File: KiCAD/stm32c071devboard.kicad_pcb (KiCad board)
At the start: 2 copper layers, 38.4 x 19.2 mm, 24 parts, among them J1 USB_C_Receptacle_USB2.0_14P, J2 Conn_01x14_Pin, J3 Conn_01x01_Pin, J4 Conn_01x14_Pin, J5 Conn_01x02_Pin, U1 STM32C071G8UxN, U3 TPS73633DBV

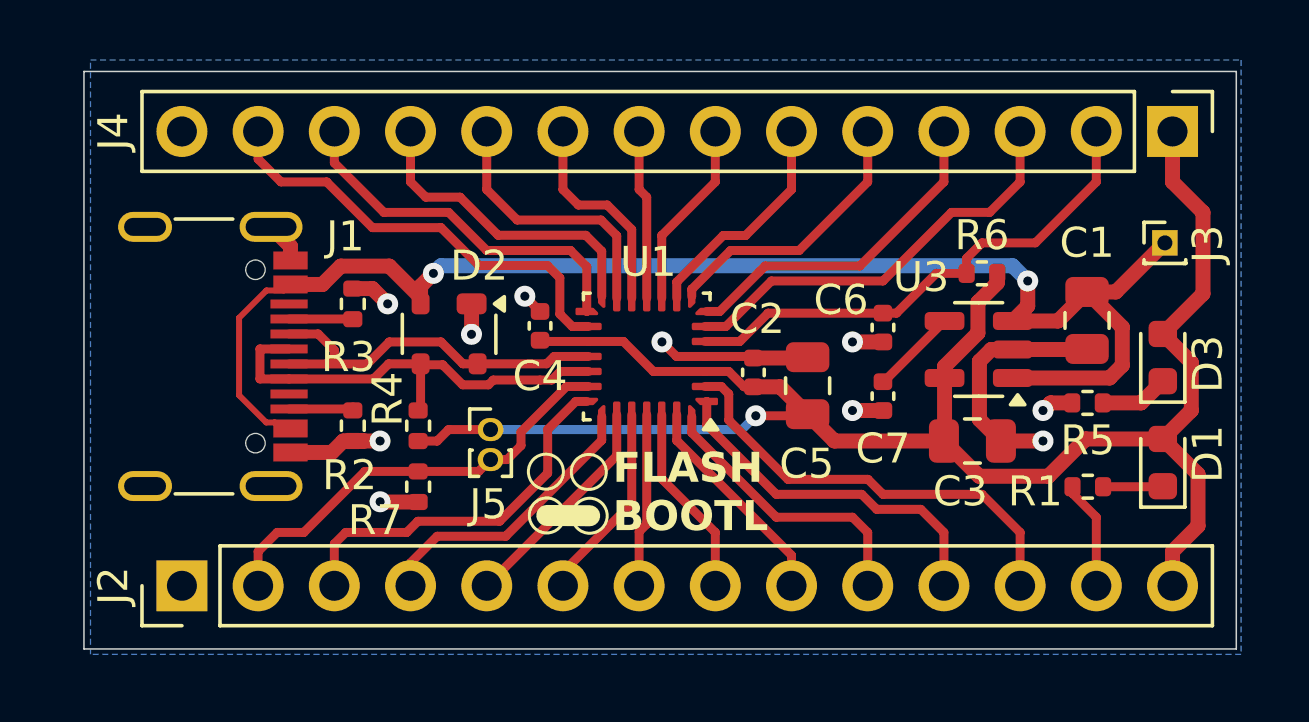
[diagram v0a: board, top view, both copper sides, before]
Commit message: Fixed 2 pins
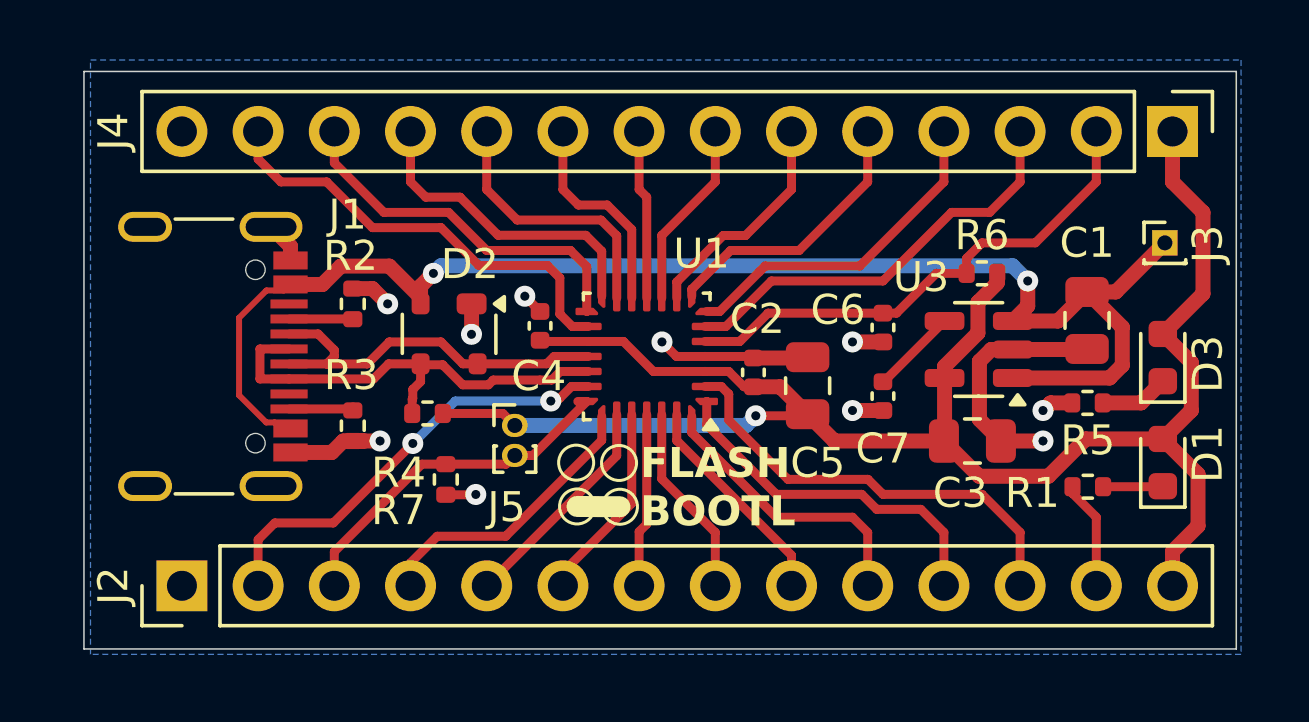
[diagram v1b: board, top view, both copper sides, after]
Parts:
- moved R7 0.95 mm to (91.6, 69.1)
- moved J5 0.82 mm to (93.9, 67.3)
- moved R4 0.52 mm to (91.0, 66.9), turned to 0 degrees
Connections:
- J2 pad 2: BOOT0 -> PA13
- J2 pad 3: PA13 -> BOOT0
- U1 pad 20: BOOT0 -> PA13
- U1 pad 21: PA13 -> BOOT0
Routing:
- net BOOT0: track 14.7 -> 11.9 mm
- net PA13: track 12.6 -> 14.9 mm, vias 0 -> 2
- net +3V3: track 60.7 -> 59.8 mm

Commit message: Minor mods
Top level ground plane and a few stitching vias
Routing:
- net GND: vias 10 -> 21
- added copper zone on F.Cu, net GND
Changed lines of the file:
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@@
+	)
+	(via
+		(at 83.525 65.278)
+		(size 0.7)
+		(drill 0.3)
+		(layers "F.Cu" "B.Cu")
+		(free yes)
+		(net 1)
 	)
 	(via
@@
 	)
 	(via
+		(at 80.985 67.818)
+		(size 0.7)
+		(drill 0.3)
+		(layers "F.Cu" "B.Cu")
+		(free yes)
+		(net 1)
+	)
+	(via
 		(at 111.506 66.802)
 		(size 0.7)
@@
 	)
 	(via
+		(at 83.525 67.818)
+		(size 0.7)
+		(drill 0.3)
+		(layers "F.Cu" "B.Cu")
+		(free yes)
+		(net 1)
+	)
+	(via
 		(at 98.806 64.516)
 		(size 0.7)
@@
 	)
 	(via
+		(at 83.525 62.738)
+		(size 0.7)
+		(drill 0.3)
+		(layers "F.Cu" "B.Cu")
+		(free yes)
+		(net 1)
+	)
+	(via
 		(at 89.662 63.246)
 		(size 0.7)
@@
 	)
 	(via
+		(at 83.525 70.358)
+		(size 0.7)
+		(drill 0.3)
+		(layers "F.Cu" "B.Cu")
+		(free yes)
+		(net 1)
+	)
+	(via
+		(at 80.985 65.278)
+		(size 0.7)
+		(drill 0.3)
+		(layers "F.Cu" "B.Cu")
+		(free yes)
+		(net 1)
+	)
+	(via
+		(at 80.985 72.898)
+		(size 0.7)
+		(drill 0.3)
+		(layers "F.Cu" "B.Cu")
+		(free yes)
+		(net 1)
+	)
+	(via
 		(at 105.156 64.516)
 		(size 0.7)
@@
 	)
 	(via
+		(at 83.525 60.198)
+		(size 0.7)
+		(drill 0.3)
+		(layers "F.Cu" "B.Cu")
+		(free yes)
+		(net 1)
+	)
+	(via
+		(at 80.985 57.658)
+		(size 0.7)
+		(drill 0.3)
+		(layers "F.Cu" "B.Cu")
+		(free yes)
+		(net 1)
+	)
+	(via
 		(at 94.234 62.992)
 		(size 0.7)
@@
 		(drill 0.3)
 		(layers "F.Cu" "B.Cu")
+		(net 1)
+	)
+	(via
+		(at 88.138 60.96)
+		(size 0.7)
+		(drill 0.3)
+		(layers "F.Cu" "B.Cu")
+		(free yes)
+		(net 1)
+	)
+	(via
+		(at 80.985 62.738)
+		(size 0.7)
+		(drill 0.3)
+		(layers "F.Cu" "B.Cu")
+		(free yes)
 		(net 1)
 	)
@@
 		(layer "F.Cu")
 		(net 36)
+	)
+	(zone
+		(net 1)
+		(net_name "GND")
+		(layer "F.Cu")
+		(hatch edge 0.5)
+		(priority 1)
+		(connect_pads
+			(clearance 0.5)
+		)
+		(min_thickness 0.25)
+		(filled_areas_thickness no)
+		(fill yes
+			(thermal_gap 0.5)
+			(thermal_bridge_width 0.5)
+		)
+		(polygon
+			(pts
+				(xy 118.364 55.118) (xy 118.364 74.676) (xy 117.856 75.184) (xy 79.248 75.184) (xy 78.74 74.676)
+				(xy 78.74 55.118)
+			)
+		)
 	)
 	(zone
@@
 		)
 	)
+	(group "ViaStitching GND"
+		(members "032abcea-ae55-4e1d-8aa3-01bf822b022d" "2fb02433-369c-49a9-9db1-dac369ce6200"
+			"4f7df9d6-2fa7-43f1-a7e0-15e366a268b4" "79157b3c-164c-4ce9-9dc7-ce8ebb17f839"
+			"9593503d-df9f-447a-a54b-ed74c478f88f" "a9d6937d-f2eb-47e0-809f-aa99a66a624d"
+			"b76ceecf-d1e5-4f90-8656-1ccb40bf2362" "d20bc4d6-5bef-49af-a551-cd1a012df23e"
+			"de0b7269-a8ad-4e2b-8983-e05780797516" "ff37f6f9-a9c4-4dcc-ac8e-5e436fae3715"
+		)
+	)
